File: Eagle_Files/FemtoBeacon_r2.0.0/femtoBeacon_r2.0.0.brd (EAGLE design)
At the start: 18 x 18 mm, 60 parts

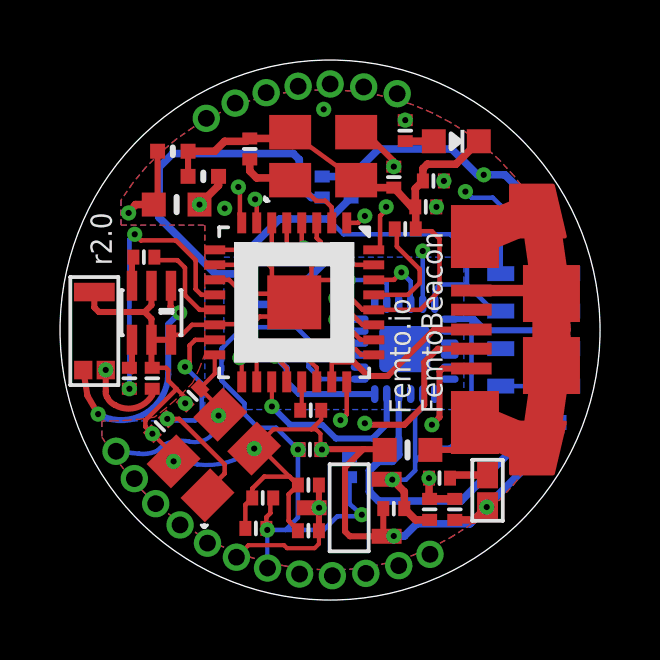
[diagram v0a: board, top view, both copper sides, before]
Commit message: Committing current work on FemtoBeacon (zigbee/mesh) r2.0.1, and USB dongle
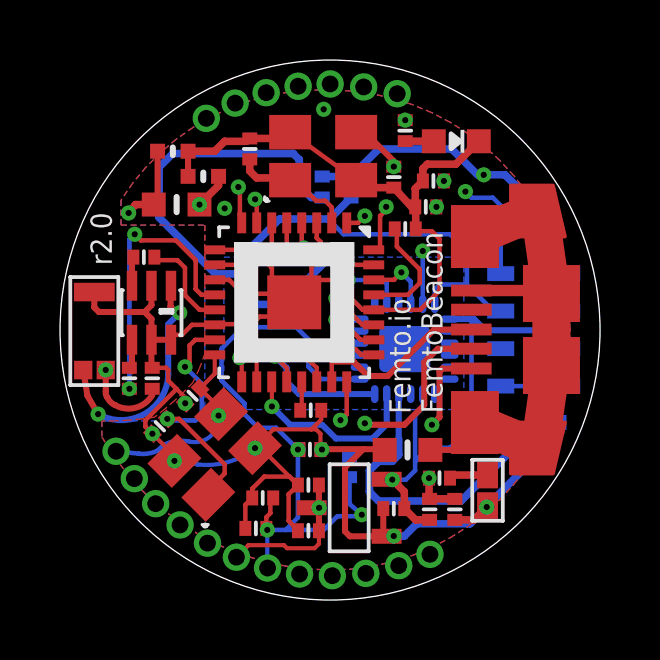
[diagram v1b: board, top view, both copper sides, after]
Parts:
- removed TSX-3225: 26MHz, crystals:TSX-3225
- removed U$8: USB_MICROB, femtoduino:USB_MICROB_PACKAGE
- added TSX-3225_CRYSTAL: 12MHz, crystals:TSX-3225
- added USB: USB_MICROB, femtoduino:USB_MICROB_PACKAGE
- C3, C4: value 9pF -> 10pF
- moved LDO_VREG 1.59 mm to (9.64, 3.07)
- moved SER3628CT-ND 1.36 mm to (8.77, 14.8)
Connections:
- net GND: now also TSX-3225_CRYSTAL.2, TSX-3225_CRYSTAL.4; no longer TSX-3225.2, TSX-3225.4
- net N$5: now also USB.10, USB.11, USB.5, USB.6, USB.7, USB.8, USB.9; no longer U$8.10, U$8.11, U$8.5, U$8.6, U$8.7, U$8.8, U$8.9
- net PA14/XIN_MC: now also TSX-3225_CRYSTAL.1; no longer TSX-3225.1
- net PA15/XOUT_MC: now also TSX-3225_CRYSTAL.3; no longer TSX-3225.3
- net PA24/USBDM: now also USB.2; no longer U$8.2
- net PA25/USBDP: now also USB.3; no longer U$8.3
- net VIN: now also USB.1; no longer U$8.1
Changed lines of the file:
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@@
 <?xml version="1.0" encoding="utf-8"?>
 <!DOCTYPE eagle SYSTEM "eagle.dtd">
-<eagle version="6.5.0">
+<eagle version="7.5.0">
 <drawing>
 <settings>
@@
 <setting verticaltext="up"/>
 </settings>
-<grid distance="2" unitdist="mil" unit="mil" style="lines" multiple="1" display="yes" altdistance="0.1" altunitdist="mm" altunit="mm"/>
+<grid distance="1" unitdist="mm" unit="mm" style="lines" multiple="1" display="yes" altdistance="0.1" altunitdist="mm" altunit="mm"/>
 <layers>
 <layer number="1" name="Top" color="4" fill="1" visible="yes" active="yes"/>
@@
 <pass name="Default">
 <param name="RoutingGrid" value="50mil"/>
+<param name="AutoGrid" value="1"/>
+<param name="Efforts" value="0"/>
+<param name="TopRouterVariant" value="1"/>
 <param name="tpViaShape" value="round"/>
 <param name="PrefDir.1" value="|"/>
@@
 </element>
 <element name="BTN" library="femtoduino" package="SPST_SMD" value="DNP" x="14.2502" y="3.6584" rot="R270"/>
-<element name="LDO_VREG" library="MCP1700T-3302E_TT" package="MCP1700T-3302E/TT" value="MCP1700T-3302E/TT" x="10.2862" y="1.6248" rot="R90"/>
+<element name="LDO_VREG" library="MCP1700T-3302E_TT" package="MCP1700T-3302E/TT" value="MCP1700T-3302E/TT" x="9.6362" y="3.0748" rot="R90"/>
 <element name="C5" library="parts_0201" package="PART" value="2.2uF" x="11.1252" y="3.048" smashed="yes" rot="R180"/>
 <element name="C6" library="parts_0201" package="PART" value="2.2uF" x="8.2796" y="3.8346" smashed="yes" rot="R180"/>
@@
 <attribute name="DIGIKEY_PART" value="490-3194-1-ND" x="6.7564" y="2.7178" size="1.778" layer="27" rot="R180" display="off"/>
 </element>
-<element name="TSX-3225" library="crystals" package="TSX-3225" value="26MHz" x="3.7846" y="4.6228" smashed="yes" rot="R45"/>
-<element name="C3" library="parts_0201" package="PART" value="9pF" x="3.3274" y="5.7912" smashed="yes" rot="R45">
+<element name="TSX-3225_CRYSTAL" library="crystals" package="TSX-3225" value="12MHz" x="5.1562" y="4.8514" smashed="yes" rot="R45"/>
+<element name="C3" library="parts_0201" package="PART" value="10pF" x="3.3274" y="5.7912" smashed="yes" rot="R45">
 <attribute name="DIGIKEY_PART" value="490-3194-1-ND" x="3.3274" y="5.7912" size="1.778" layer="27" rot="R45" display="off"/>
 </element>
-<element name="C4" library="parts_0201" package="PART" value="9pF" x="4.4196" y="6.8072" smashed="yes" rot="R225">
+<element name="C4" library="parts_0201" package="PART" value="10pF" x="4.4196" y="6.8072" smashed="yes" rot="R225">
 <attribute name="DIGIKEY_PART" value="490-3194-1-ND" x="4.4196" y="6.8072" size="1.778" layer="27" rot="R225" display="off"/>
 </element>
@@
 <attribute name="DIGIKEY_PART" value="490-3194-1-ND" x="3.0734" y="7.3914" size="1.778" layer="27" rot="R90" display="off"/>
 </element>
-<element name="SER3628CT-ND" library="crystals" package="TSX-3225" value="16MHz" x="7.6708" y="15.5956" smashed="yes"/>
+<element name="SER3628CT-ND" library="crystals" package="TSX-3225" value="16MHz" x="8.7708" y="14.7956" smashed="yes"/>
 <element name="C14" library="parts_0201" package="PART" value="9pF" x="6.3246" y="15.0368" smashed="yes" rot="R270">
 <attribute name="DIGIKEY_PART" value="490-3194-1-ND" x="6.3246" y="15.0368" size="1.778" layer="27" rot="R270" display="off"/>
@@
 <attribute name="DIGIKEY_PART" value="490-3194-1-ND" x="16.3322" y="5.9182" size="1.778" layer="28" rot="MR180" display="off"/>
 </element>
-<element name="U$8" library="femtoduino" package="USB_MICROB_PACKAGE" value="USB_MICROB" x="13.0302" y="9.017" rot="R90"/>
+<element name="USB" library="femtoduino" package="USB_MICROB_PACKAGE" value="USB_MICROB" x="15.1802" y="9.017" rot="R90"/>
 <element name="FB1" library="microbuilder" package="_0603MP" value="" x="11.5824" y="5.0038" smashed="yes" rot="R180">
 <attribute name="VALUE" x="12.5349" y="5.9563" size="0.4064" layer="27" ratio="10" rot="R180"/>
@@
 <signal name="PA14/XIN_MC">
 <contactref element="U$76" pad="15"/>
-<contactref element="TSX-3225" pad="1"/>
+<contactref element="TSX-3225_CRYSTAL" pad="1"/>
 <contactref element="C3" pad="2"/>
 <wire x1="3.968915625" y1="6.038684375" x2="5.4864" y2="4.5212" width="0.1524" layer="1"/>
 <wire x1="5.4864" y1="4.5212" x2="5.4864" y2="4.2164" width="0.1524" layer="1"/>
 <wire x1="5.4864" y1="4.2164" x2="4.91596875" y2="3.64596875" width="0.1524" layer="1"/>
-<wire x1="4.91596875" y1="3.64596875" x2="4.91596875" y2="3.491428125" width="0.1524" layer="1"/>
+<wire x1="4.91596875" y1="3.64596875" x2="4.944065625" y2="3.507896875" width="0.1524" layer="1"/>
 <wire x1="5.1562" y1="8.673" x2="4.5074" y2="8.673" width="0.1524" layer="1"/>
 <wire x1="4.5074" y1="8.673" x2="4.318" y2="8.4836" width="0.1524" layer="1"/>
@@
 <contactref element="U$76" pad="16"/>
 <contactref element="U$39" pad="P$1"/>
-<contactref element="TSX-3225" pad="3"/>
+<contactref element="TSX-3225_CRYSTAL" pad="3"/>
 <contactref element="C4" pad="1"/>
 <wire x1="5.1562" y1="8.173" x2="5.1562" y2="7.5438" width="0.1397" layer="1"/>
 <wire x1="5.1562" y1="7.5438" x2="4.667084375" y2="7.054684375" width="0.1397" layer="1"/>
-<wire x1="5.340234375" y1="6.178434375" x2="5.3086" y2="6.1468" width="0.1397" layer="1"/>
+<wire x1="5.36833125" y1="6.1949" x2="5.3086" y2="6.1468" width="0.1397" layer="1"/>
 <wire x1="5.3086" y1="6.1468" x2="5.2832" y2="6.1468" width="0.1397" layer="1"/>
 <via x="5.2832" y="6.1468" extent="1-16" drill="0.2032" diameter="0.508"/>
@@
 <contactref element="U$9" pad="P$1"/>
 <contactref element="U$76" pad="22"/>
-<contactref element="U$8" pad="2"/>
+<contactref element="USB" pad="2"/>
 <wire x1="8.5562" y1="7.273" x2="8.5562" y2="7.7506" width="0.1397" layer="1"/>
 <wire x1="8.5562" y1="7.7506" x2="7.7724" y2="8.4328" width="0.1397" layer="1"/>
@@
 <contactref element="U$10" pad="P$1"/>
 <contactref element="U$76" pad="23"/>
-<contactref element="U$8" pad="3"/>
+<contactref element="USB" pad="3"/>
 <wire x1="13.7102" y1="9.017" x2="12.4714" y2="9.017" width="0.2032" layer="1"/>
 <wire x1="12.4714" y1="9.017" x2="10.922" y2="7.4676" width="0.2032" layer="1"/>
@@
 <contactref element="U$76" pad="14"/>
 <contactref element="C10" pad="2"/>
-<contactref element="TSX-3225" pad="2"/>
-<contactref element="TSX-3225" pad="4"/>
+<contactref element="TSX-3225_CRYSTAL" pad="2"/>
+<contactref element="TSX-3225_CRYSTAL" pad="4"/>
 <contactref element="C3" pad="1"/>
 <contactref element="C4" pad="2"/>
@@
 <wire x1="3.048" y1="8.6758" x2="3.698" y2="8.6758" width="0.2032" layer="1"/>
 <wire x1="4.2672" y1="14.9606" x2="4.2672" y2="14.1224" width="0.2032" layer="1"/>
-<via x="3.7846" y="4.6228" extent="1-16" drill="0.2032" diameter="0.508"/>
-<via x="6.471603125" y="5.0470625" extent="1-16" drill="0.2032" diameter="0.508"/>
+<via x="3.812696875" y="4.639265625" extent="1-16" drill="0.2032" diameter="0.508"/>
+<via x="6.4997" y="5.06353125" extent="1-16" drill="0.2032" diameter="0.508"/>
 <wire x1="5.1562" y1="9.173" x2="5.178" y2="9.1948" width="0.1397" layer="1"/>
 <wire x1="5.178" y1="9.1948" x2="6.4008" y2="9.1948" width="0.1524" layer="1"/>
@@
 <wire x1="4.1721125" y1="6.7498875" x2="4.1721125" y2="6.5597125" width="0.1397" layer="1"/>
 <wire x1="3.0799125" y1="5.5437125" x2="3.7846" y2="4.839025" width="0.1397" layer="1"/>
-<wire x1="3.7846" y1="4.839025" x2="3.7846" y2="4.6228" width="0.1397" layer="1"/>
-<wire x1="3.7846" y1="4.6228" x2="4.572" y2="4.5212" width="0.1397" layer="16"/>
-<wire x1="4.572" y1="4.5212" x2="6.471603125" y2="5.0470625" width="0.1397" layer="16" curve="45.652032"/>
-<wire x1="6.471603125" y1="5.0470625" x2="6.7171375" y2="5.0470625" width="0.1397" layer="1"/>
+<wire x1="3.7846" y1="4.839025" x2="3.812696875" y2="4.639265625" width="0.1397" layer="1"/>
+<wire x1="3.812696875" y1="4.639265625" x2="4.572" y2="4.5212" width="0.1397" layer="16"/>
+<wire x1="4.572" y1="4.5212" x2="6.4997" y2="5.06353125" width="0.1397" layer="16" curve="45.652032"/>
+<wire x1="6.4997" y1="5.06353125" x2="6.7171375" y2="5.0470625" width="0.1397" layer="1"/>
 <wire x1="6.7171375" y1="5.0470625" x2="7.9296" y2="3.8346" width="0.1397" layer="1"/>
 <via x="8.7312" y="5.0157" extent="1-16" drill="0.2032" diameter="0.508"/>
@@
 <wire x1="8.5344" y1="5.6896" x2="8.382" y2="5.6896" width="0.1397" layer="1"/>
 <wire x1="8.382" y1="5.6896" x2="7.114140625" y2="5.6896" width="0.1397" layer="1"/>
-<wire x1="7.114140625" y1="5.6896" x2="6.471603125" y2="5.0470625" width="0.1397" layer="1"/>
+<wire x1="7.114140625" y1="5.6896" x2="6.4997" y2="5.06353125" width="0.1397" layer="1"/>
 <wire x1="8.7066" y1="6.3246" x2="8.7066" y2="6.0142" width="0.1397" layer="1"/>
 <wire x1="8.7066" y1="6.0142" x2="8.382" y2="5.6896" width="0.1397" layer="1"/>
@@
 <contactref element="C7" pad="1"/>
 <contactref element="U$1" pad="P$1"/>
-<contactref element="U$8" pad="1"/>
+<contactref element="USB" pad="1"/>
 <wire x1="8.6296" y1="2.3106" x2="8.6296" y2="1.8732" width="0.1397" layer="1"/>
 <wire x1="8.6296" y1="1.8732" x2="8.4836" y2="1.7272" width="0.1397" layer="1"/>
@@
 </signal>
 <signal name="N$5">
-<contactref element="U$8" pad="6"/>
-<contactref element="U$8" pad="11"/>
-<contactref element="U$8" pad="7"/>
-<contactref element="U$8" pad="8"/>
-<contactref element="U$8" pad="9"/>
-<contactref element="U$8" pad="10"/>
-<contactref element="U$8" pad="5"/>
+<contactref element="USB" pad="6"/>
+<contactref element="USB" pad="11"/>
+<contactref element="USB" pad="7"/>
+<contactref element="USB" pad="8"/>
+<contactref element="USB" pad="9"/>
+<contactref element="USB" pad="10"/>
+<contactref element="USB" pad="5"/>
 <contactref element="FB1" pad="1"/>
 <wire x1="12.3444" y1="5.0038" x2="13.2726" y2="5.0038" width="0.2032" layer="1"/>
